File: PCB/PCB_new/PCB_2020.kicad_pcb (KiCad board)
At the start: 2 copper layers, 102.2 x 94.5 mm, 26 parts, among them IC1 LM358N, Q1 220mA/50V/3.5Ω, Q2 100V/17A, Q3 100V/17A, Q4 100V/17A, Q5 100V/17A, Q6 100V/17A, U1 TI_CONN

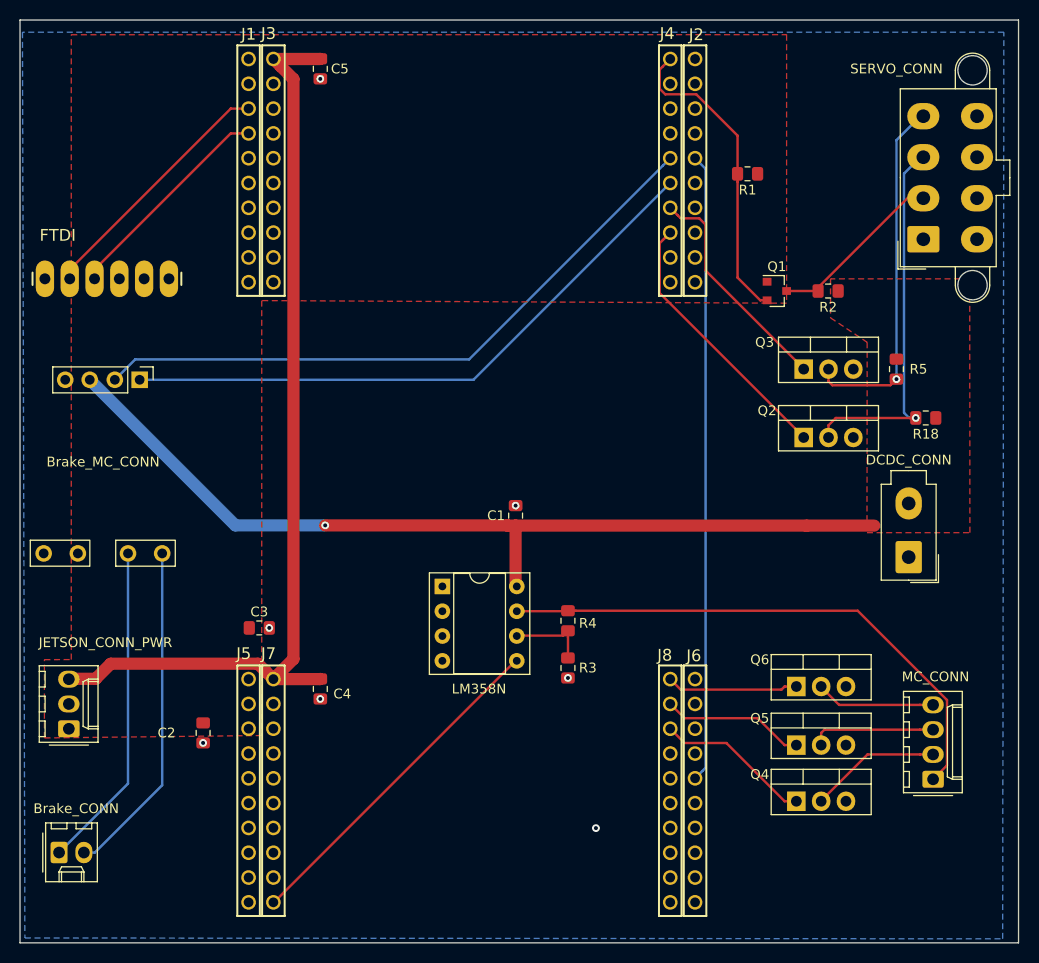
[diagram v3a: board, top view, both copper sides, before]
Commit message: moved vias from component pads
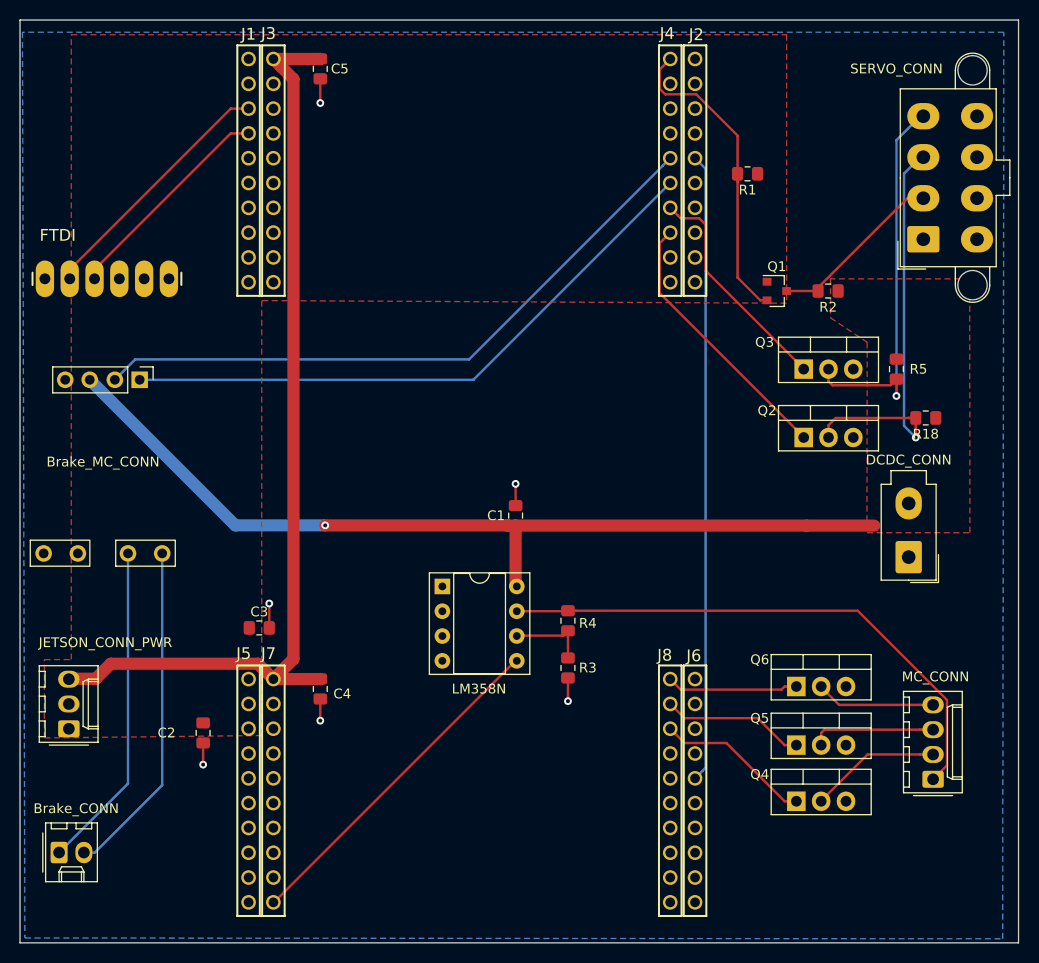
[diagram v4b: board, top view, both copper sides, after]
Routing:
- net GND: track 0.00 -> 14.0 mm, vias 7 -> 6
- net /LAUNCHXL-F28379D Breakout/INPUT_A+: track 39.8 -> 43.4 mm
- net /LAUNCHXL-F28379D Breakout/EN+: track 36.9 -> 40.3 mm
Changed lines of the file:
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@@
     (thickness 1.6)
     (drawings 1)
-    (tracks 136)
+    (tracks 143)
     (zones 0)
     (modules 26)
@@
     (add_net "/LAUNCHXL-F28379D Breakout/REV_MC")
     (add_net "/LAUNCHXL-F28379D Breakout/THROTTLE_MC")
-    (add_net "/LAUNCHXL-F28379D Headers/ADCA0")
-    (add_net "/LAUNCHXL-F28379D Headers/ADCIN1")
-    (add_net "/LAUNCHXL-F28379D Headers/ADCIN15")
-    (add_net "/LAUNCHXL-F28379D Headers/ADCINA2")
-    (add_net "/LAUNCHXL-F28379D Headers/ADCINA3")
-    (add_net "/LAUNCHXL-F28379D Headers/ADCINA4")
-    (add_net "/LAUNCHXL-F28379D Headers/ADCINA5")
-    (add_net "/LAUNCHXL-F28379D Headers/ADCINB2")
-    (add_net "/LAUNCHXL-F28379D Headers/ADCINB3")
-    (add_net "/LAUNCHXL-F28379D Headers/ADCINB4")
-    (add_net "/LAUNCHXL-F28379D Headers/ADCINB5")
-    (add_net "/LAUNCHXL-F28379D Headers/ADCINC2")
-    (add_net "/LAUNCHXL-F28379D Headers/ADCINC3")
-    (add_net "/LAUNCHXL-F28379D Headers/ADCINC4")
-    (add_net "/LAUNCHXL-F28379D Headers/ADCINC5")
-    (add_net "/LAUNCHXL-F28379D Headers/GPIO1-PWMOUT1B")
-    (add_net "/LAUNCHXL-F28379D Headers/GPIO104-I2CSDAA-J1")
-    (add_net "/LAUNCHXL-F28379D Headers/GPIO105-I2SSCLA-J1")
-    (add_net "/LAUNCHXL-F28379D Headers/GPIO111")
-    (add_net "/LAUNCHXL-F28379D Headers/GPIO122-SD1D1")
-    (add_net "/LAUNCHXL-F28379D Headers/GPIO123-SD1CLK1")
-    (add_net "/LAUNCHXL-F28379D Headers/GPIO124-SD1D2")
-    (add_net "/LAUNCHXL-F28379D Headers/GPIO125-SD1CLK2")
-    (add_net "/LAUNCHXL-F28379D Headers/GPIO130-SD2D1")
-    (add_net "/LAUNCHXL-F28379D Headers/GPIO131-SD2CLK1")
-    (add_net "/LAUNCHXL-F28379D Headers/GPIO139-SCICRX(->MCU)")
-    (add_net "/LAUNCHXL-F28379D Headers/GPIO15-OPXBAR4")
-    (add_net "/LAUNCHXL-F28379D Headers/GPIO2-PWMOUT2A")
-    (add_net "/LAUNCHXL-F28379D Headers/GPIO22")
-    (add_net "/LAUNCHXL-F28379D Headers/GPIO25-OPXBAR2")
-    (add_net "/LAUNCHXL-F28379D Headers/GPIO26-SD2D2")
-    (add_net "/LAUNCHXL-F28379D Headers/GPIO27-SD2CLK2")
-    (add_net "/LAUNCHXL-F28379D Headers/GPIO29-OPXBAR6")
-    (add_net "/LAUNCHXL-F28379D Headers/GPIO3-PWMOUT2B")
-    (add_net "/LAUNCHXL-F28379D Headers/GPIO32")
-    (add_net "/LAUNCHXL-F28379D Headers/GPIO52-J5")
-    (add_net "/LAUNCHXL-F28379D Headers/GPIO56-SCICTX(<-MCU)")
-    (add_net "/LAUNCHXL-F28379D Headers/GPIO58-SPIAMOSI")
-    (add_net "/LAUNCHXL-F28379D Headers/GPIO59-SPIAMISO")
-    (add_net "/LAUNCHXL-F28379D Headers/GPIO60-SPICLKA")
-    (add_net "/LAUNCHXL-F28379D Headers/GPIO61-SPIACS")
-    (add_net "/LAUNCHXL-F28379D Headers/GPIO63-SPIBMOSI")
-    (add_net "/LAUNCHXL-F28379D Headers/GPIO64-SPIBMISO")
-    (add_net "/LAUNCHXL-F28379D Headers/GPIO65-SPIBCLK")
-    (add_net "/LAUNCHXL-F28379D Headers/GPIO66-SPIBCS")
-    (add_net "/LAUNCHXL-F28379D Headers/GPIO67")
-    (add_net "/LAUNCHXL-F28379D Headers/GPIO94")
-    (add_net "/LAUNCHXL-F28379D Headers/PWM-BASED-DAC1")
-    (add_net "/LAUNCHXL-F28379D Headers/PWM-BASED-DAC2")
-    (add_net "/LAUNCHXL-F28379D Headers/PWM-BASED-DAC3")
-    (add_net "/LAUNCHXL-F28379D Headers/PWM-BASED-DAC4")
     (add_net "/LAUNCHXL-F28379D Headers/RESET")
     (add_net Brake_PWM_1)
@@
     (add_net GND)
     (add_net INPUT_A+_CTL)
-    (add_net "Net-(CONN1-Pad1)")
-    (add_net "Net-(CONN1-Pad5)")
     (add_net "Net-(IC1-Pad6)")
-    (add_net "Net-(U1-Pad42)")
-    (add_net "Net-(U1-Pad45)")
-    (add_net "Net-(U1-Pad49)")
-    (add_net "Net-(U1-Pad50)")
-    (add_net "Net-(U1-Pad75)")
-    (add_net "Net-(U1-Pad76)")
-    (add_net "Net-(U1-Pad77)")
     (add_net REV_CTL)
     (add_net SCIB_RX)
@@
   (segment (start 123.75 112.186) (end 123.75 52.796) (width 1.25) (layer Top) (net 2))
   (segment (start 121.695 114.241) (end 123.75 112.186) (width 1.25) (layer Top) (net 2))
-  (via (at 151.86 114.126) (size 0.8) (drill 0.4) (layers Top Bottom) (net 3))
-  (via (at 146.5 96.475) (size 0.8) (drill 0.4) (layers Top Bottom) (net 3))
-  (via (at 126.5 116.275) (size 0.8) (drill 0.4) (layers Top Bottom) (net 3))
-  (via (at 114.5 120.775) (size 0.8) (drill 0.4) (layers Top Bottom) (net 3))
-  (via (at 126.5 52.775) (size 0.8) (drill 0.4) (layers Top Bottom) (net 3))
-  (via (at 121.275 109) (size 0.8) (drill 0.4) (layers Top Bottom) (net 3))
-  (via (at 154.725 129.5) (size 0.8) (drill 0.4) (layers Top Bottom) (net 3))
+  (via (at 151.86 116.5) (size 0.8) (drill 0.4) (layers Top Bottom) (net 3))
+  (via (at 146.5 94.25) (size 0.8) (drill 0.4) (layers Top Bottom) (net 3))
+  (via (at 126.5 118.5) (size 0.8) (drill 0.4) (layers Top Bottom) (net 3))
+  (via (at 114.5 123) (size 0.8) (drill 0.4) (layers Top Bottom) (net 3))
+  (via (at 126.5 55.25) (size 0.8) (drill 0.4) (layers Top Bottom) (net 3))
+  (via (at 121.275 106.5) (size 0.8) (drill 0.4) (layers Top Bottom) (net 3))
+  (segment (start 151.86 114.126) (end 151.86 116.5) (width 0.25) (layer Top) (net 3))
+  (segment (start 126.5 116.275) (end 126.5 118.5) (width 0.25) (layer Top) (net 3))
+  (segment (start 114.5 120.775) (end 114.5 123) (width 0.25) (layer Top) (net 3))
+  (segment (start 121.275 106.5) (end 121.275 109) (width 0.25) (layer Top) (net 3))
+  (segment (start 126.5 52.775) (end 126.5 55.25) (width 0.25) (layer Top) (net 3))
+  (segment (start 146.5 94.25) (end 146.5 96.475) (width 0.25) (layer Top) (net 3))
   (segment (start 121.755 137.101) (end 121.695 137.101) (width 0.25) (layer Top) (net 4))
   (segment (start 146.526 112.33) (end 121.755 137.101) (width 0.25) (layer Top) (net 4))
@@
   (segment (start 178.938372 84.148372) (end 184.876628 84.148372) (width 0.25) (layer Top) (net 16))
   (segment (start 184.876628 84.148372) (end 185.5 83.525) (width 0.25) (layer Top) (net 16))
-  (via (at 185.5 83.525) (size 0.8) (drill 0.4) (layers Top Bottom) (net 16))
+  (via (at 185.5 85.25) (size 0.8) (drill 0.4) (layers Top Bottom) (net 16))
+  (segment (start 185.5 83.525) (end 185.5 85.25) (width 0.25) (layer Top) (net 16))
+  (segment (start 185.5 83.525) (end 185.5 85.25) (width 0.25) (layer Bottom) (net 16))
   (segment (start 179.29 87.5) (end 187.475 87.5) (width 0.25) (layer Top) (net 17))
-  (segment (start 186.8 87.5) (end 187.475 87.5) (width 0.25) (layer Bottom) (net 17))
-  (segment (start 186.27499 86.97499) (end 186.8 87.5) (width 0.25) (layer Bottom) (net 17))
   (segment (start 186.8 87.5) (end 187.475 87.5) (width 0.25) (layer Top) (net 17))
-  (segment (start 186.27499 62.47501) (end 187.95 60.8) (width 0.25) (layer Bottom) (net 17))
   (segment (start 178.54 89.5) (end 178.54 88.25) (width 0.25) (layer Top) (net 17))
   (segment (start 178.54 88.25) (end 179.29 87.5) (width 0.25) (layer Top) (net 17))
-  (segment (start 186.27499 86.97499) (end 186.27499 62.47501) (width 0.25) (layer Bottom) (net 17))
+  (via (at 187.475 89.5) (size 0.8) (drill 0.4) (layers Top Bottom) (net 17))
+  (segment (start 187.475 87.5) (end 187.475 89.5) (width 0.25) (layer Top) (net 17))
   (segment (start 187.95 60.8) (end 188.25 60.8) (width 0.25) (layer Bottom) (net 17))
-  (via (at 187.475 87.5) (size 0.8) (drill 0.4) (layers Top Bottom) (net 17))
+  (segment (start 186.27499 62.47501) (end 187.95 60.8) (width 0.25) (layer Bottom) (net 17))
+  (segment (start 186.27499 88.29999) (end 186.27499 62.47501) (width 0.25) (layer Bottom) (net 17))
+  (segment (start 187.475 89.5) (end 186.27499 88.29999) (width 0.25) (layer Bottom) (net 17))
   (segment (start 186.78 64.838) (end 177.475 74.143) (width 0.25) (layer Top) (net 18))
   (segment (start 174.35 74.5) (end 177.475 74.5) (width 0.25) (layer Top) (net 18))

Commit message: added 3 to 12 volt conversion circuit for braking PWM
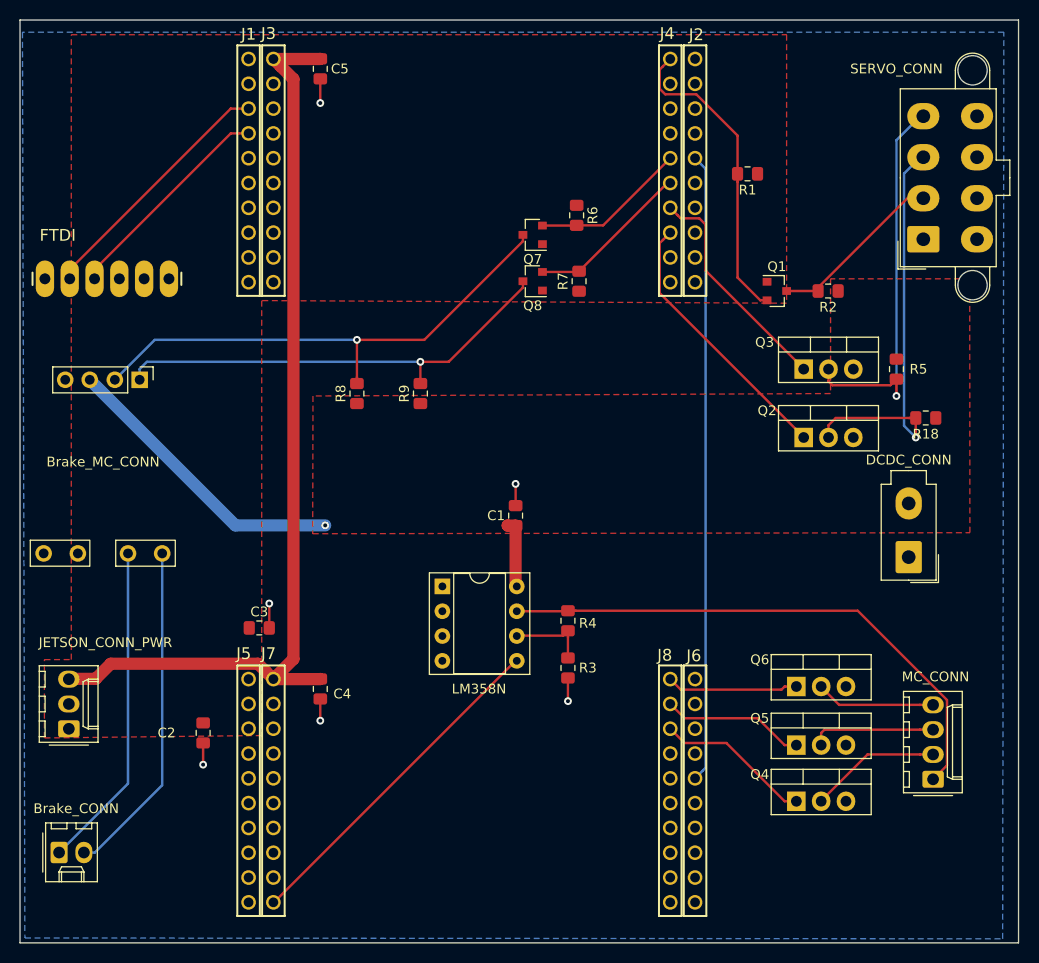
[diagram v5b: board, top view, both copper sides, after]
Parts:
- added Q7: 220mA/50V/3.5Ω, Package_TO_SOT_SMD:SOT-23, F.Cu at (148.2, 68.8)
- added Q8: 220mA/50V/3.5Ω, Package_TO_SOT_SMD:SOT-23, F.Cu at (148.2, 73.5)
- added R6: 10k, Resistor_SMD:R_0805_2012Metric_Pad1.15x1.40mm_HandSolder, F.Cu at (152.8, 66.8)
- added R7: 10k, Resistor_SMD:R_0805_2012Metric_Pad1.15x1.40mm_HandSolder, F.Cu at (153.0, 73.5)
- added R8: 10k, Resistor_SMD:R_0805_2012Metric_Pad1.15x1.40mm_HandSolder, F.Cu at (130.2, 85.0)
- added R9: 10k, Resistor_SMD:R_0805_2012Metric_Pad1.15x1.40mm_HandSolder, F.Cu at (136.8, 85.0)
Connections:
- CONN6 pad 1: Brake_PWM_2 -> /LAUNCHXL-F28379D Breakout/Brake_Ctr_2
- CONN6 pad 2: Brake_PWM_1 -> /LAUNCHXL-F28379D Breakout/Brake_Ctr_1
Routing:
- net +12V: track 92.7 -> 37.3 mm
- net /LAUNCHXL-F28379D Breakout/Brake_Ctr_1: track 0.00 -> 53.5 mm, vias 0 -> 1
- net Brake_PWM_1: track 66.3 -> 15.9 mm
- net /LAUNCHXL-F28379D Breakout/Brake_Ctr_2: track 0.00 -> 46.7 mm, vias 0 -> 1
- net Brake_PWM_2: track 62.7 -> 16.9 mm
